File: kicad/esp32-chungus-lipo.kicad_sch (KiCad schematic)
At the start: 17 parts, among them J1 USB_B_Micro, J2 Conn_01x02, J3 Conn_01x11, J4 Conn_01x11, U1 ESP32-S3-WROOM-1, U2 MAX1551EZK+T, U3 RT9080-33GJ5, U4 WS2812B

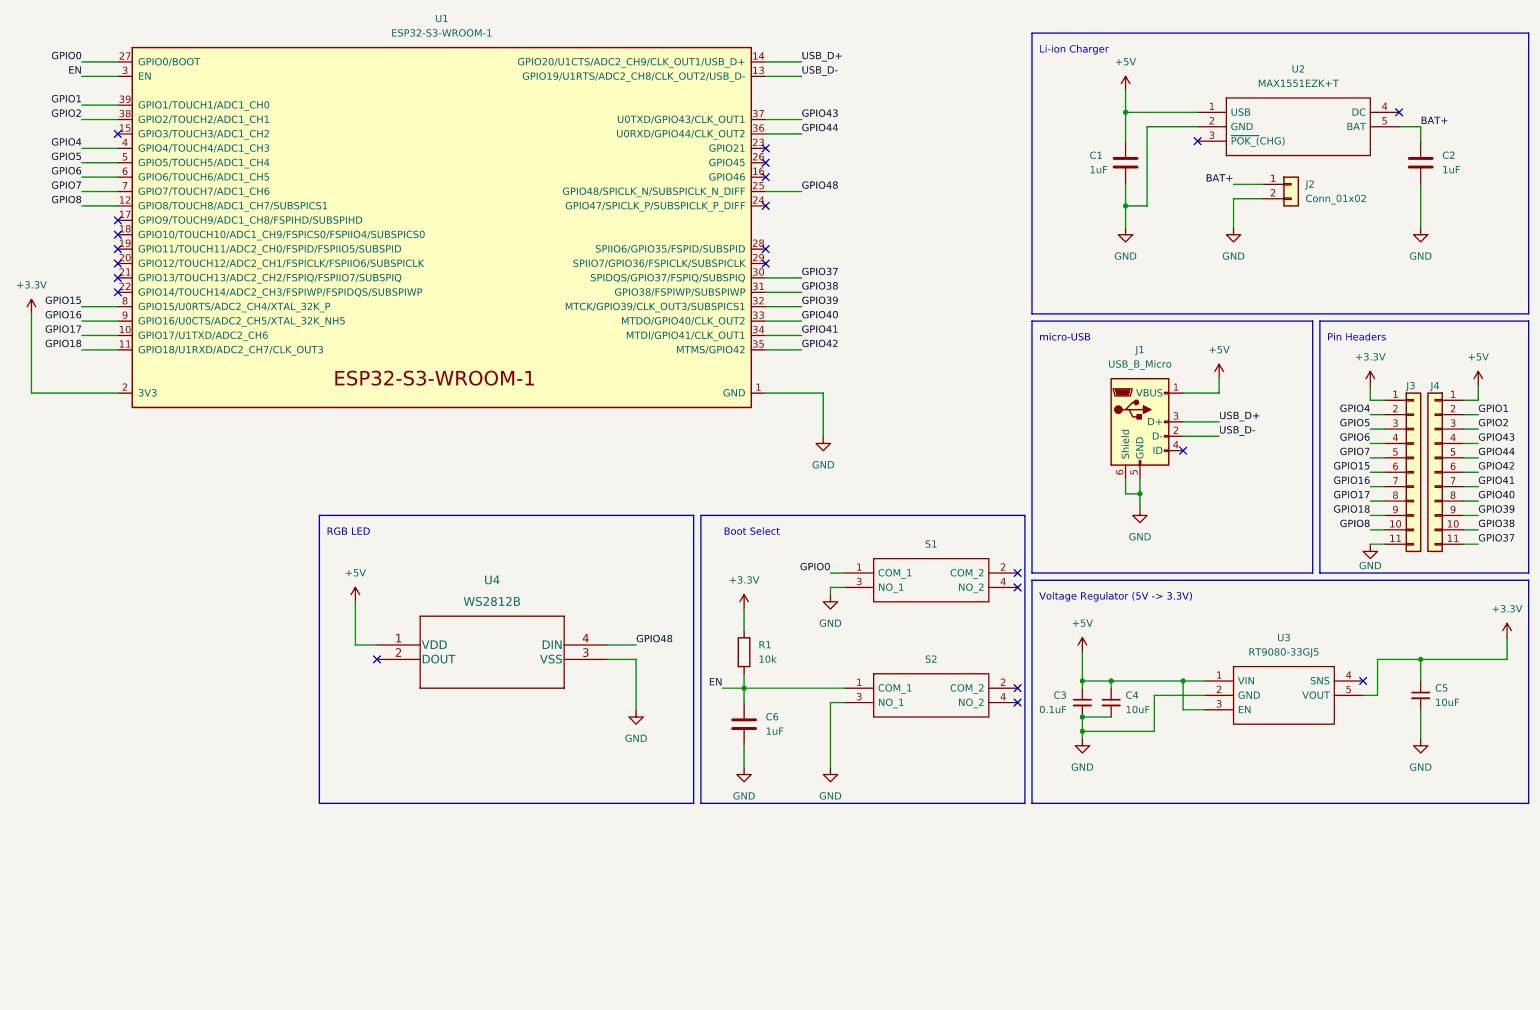
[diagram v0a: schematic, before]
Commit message: add r2 lipo with fix to power circuit
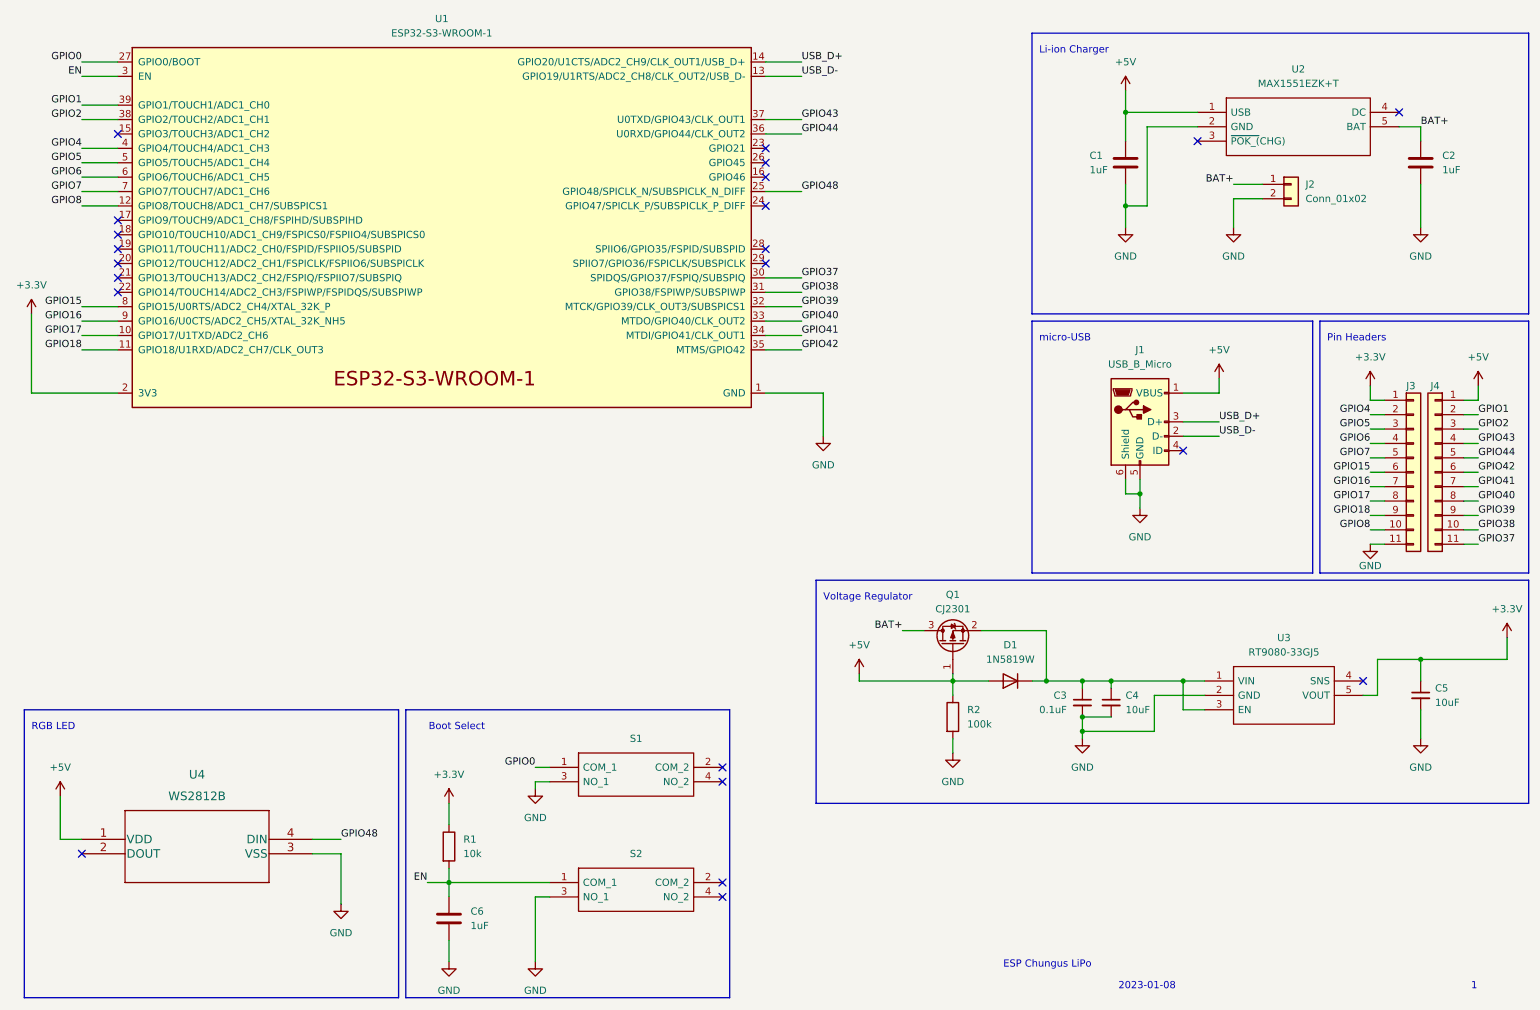
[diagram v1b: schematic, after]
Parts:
- added D1: 1N5819W, Diode_SMD:D_0603_1608Metric, symbol Device:D
- added Q1: CJ2301, Package_TO_SOT_SMD:SOT-23, symbol Device:Q_PMOS_GSD
- added R2: 100k, Resistor_SMD:R_0603_1608Metric, symbol Device:R
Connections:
- net +5V: now also D1.2 (A), Q1.1 (G), R2.1; no longer C3.1, C4.1, U3.1 (VIN), U3.3 (EN)
- net BAT+: now also Q1.3 (D)
- net GND: now also R2.2
- new net: C3.1, C4.1, D1.1 (K), Q1.2 (S), U3.1 (VIN), U3.3 (EN)
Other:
- note added: "1"
- note added: "2023-01-08"
- note added: "ESP Chungus LiPo"
- note added: "Voltage Regulator"
- note removed: "Voltage Regulator (5V -> 3.3V)"
- moved on the sheet: C6, R1, S1, S2, U4
